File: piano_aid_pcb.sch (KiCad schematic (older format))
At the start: 35 parts, among them J1 Barrel_Jack_MountingPin, J2 796644-3, J3 DIN-5_180degree, J4 Conn_01x06_Female, J5 Micro_SD_Card_Det, J6 Conn_01x07_Female, U1 317030213, U2 6N138, U3 74AHCT1G125W5-7, U4 AZ1117-3.3

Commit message: Made some adjustments. Fixed silkscreen. Added team info.
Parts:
- J1: symbol Connector:Barrel_Jack_MountingPin -> piano_aid_pcb-rescue:Barrel_Jack_MountingPin-Connector
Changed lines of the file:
@@
 $EndComp
 $Comp
-L Connector:Barrel_Jack_MountingPin J1
+L piano_aid_pcb-rescue:Barrel_Jack_MountingPin-Connector J1
 U 1 1 61503033
 P 1150 1350

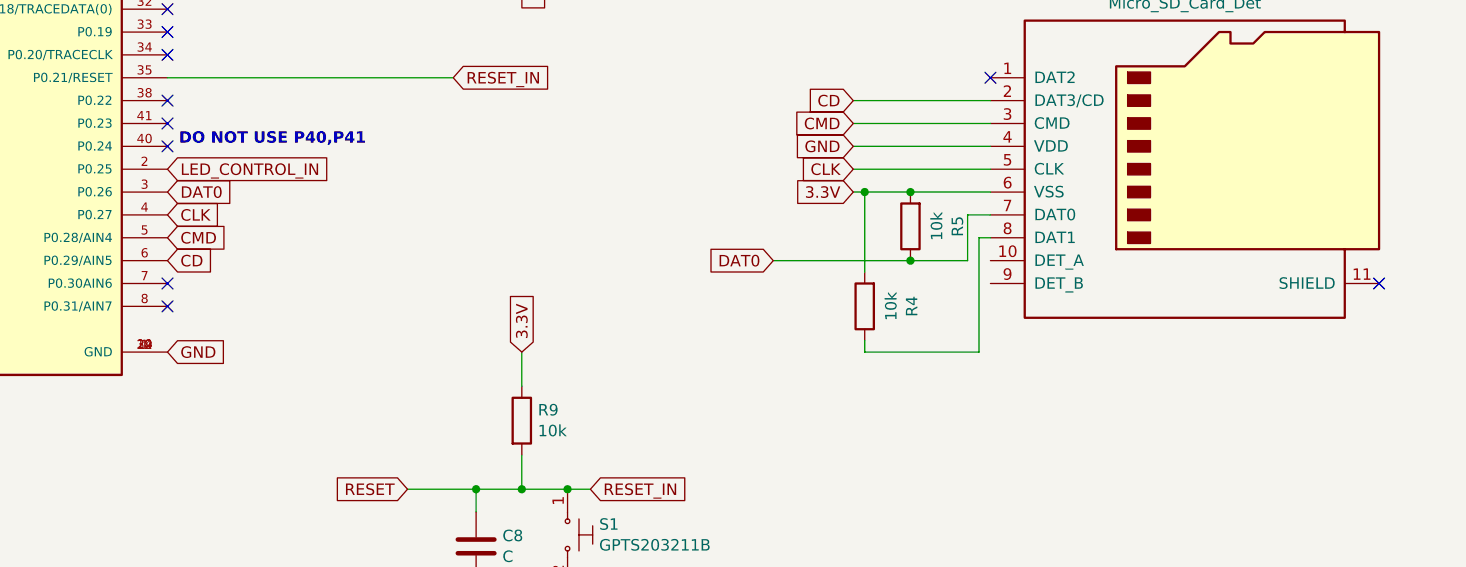
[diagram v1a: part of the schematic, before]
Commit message: Fixed some silkscreen issues. Also fixed microsd footprint and added chip detect functionality
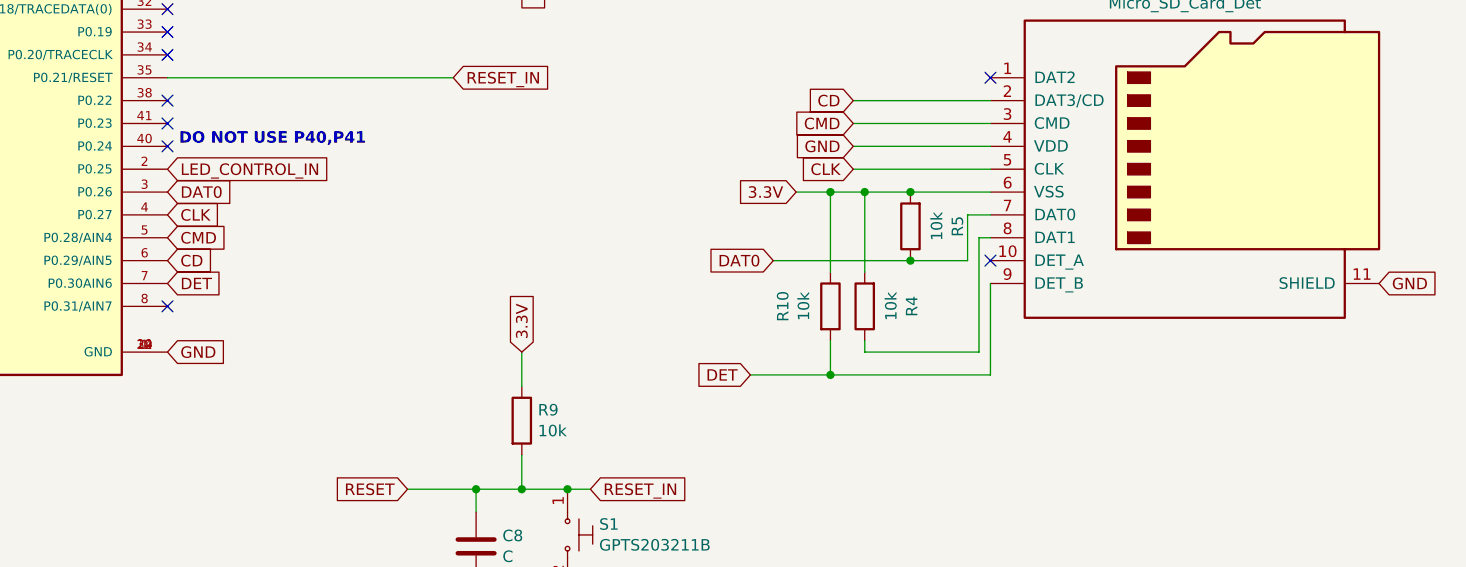
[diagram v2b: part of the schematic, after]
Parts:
- added R10: 10k, Resistor_SMD:R_0805_2012Metric_Pad1.15x1.40mm_HandSolder, symbol Device:R
- J5: footprint adafruit:MICROSD -> microsd:MICROSD
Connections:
- net 3.3V: now also R10.1
- net GND: now also J5.11 (SHIELD)
- net DET: now reaches U1.7 (P0.30AIN6)
- net DET: now also J5.9 (DET_B), R10.2
- no-connect marks 23 -> 22
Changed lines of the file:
@@
 Connection ~ 1700 1500
 Connection ~ 1700 1200
-Text GLabel 8650 4200 0    50   Input ~ 0
+Text GLabel 8400 4200 0    50   Input ~ 0
 3.3V
 Text GLabel 5900 2500 2    50   Input ~ 0
@@
 Wire Wire Line
 	8650 4000 9250 4000
-Wire Wire Line
-	8650 4200 8700 4200
 Connection ~ 8900 4200
 NoConn ~ 9250 3700
@@
 NoConn ~ 5650 3300
 NoConn ~ 5650 3800
-NoConn ~ 5650 4600
 NoConn ~ 5650 4700
 NoConn ~ 3650 3700
@@
 NoConn ~ 5650 2700
 NoConn ~ 5650 2600
-NoConn ~ 10950 4600
 Wire Wire Line
 	7250 2500 7650 2500
@@
 F 3 "~" H 1200 1310 50  0001 C CNN
 	1    1150 1350
-	1    0    0    -1
-$EndComp
-$Comp
-L Connector:Micro_SD_Card_Det J5
-U 1 1 61510C4F
-P 10150 4100
-F 0 "J5" H 10100 4917 50  0000 C CNN
-F 1 "Micro_SD_Card_Det" H 10100 4826 50  0000 C CNN
-F 2 "adafruit:MICROSD" H 12200 4800 50  0001 C CNN
-F 3 "https://www.hirose.com/product/en/download_file/key_name/DM3/category/Catalog/doc_file_id/49662/?file_category_id=4&item_id=195&is_series=1" H 10150 4200 50  0001 C CNN
-	1    10150 4100
 	1    0    0    -1
 $EndComp
@@
 	1    0    0    -1
 $EndComp
+NoConn ~ 9250 4500
+$Comp
+L Device:R R10
+U 1 1 6157C549
+P 8550 4700
+F 0 "R10" V 8343 4700 50  0000 C CNN
+F 1 "10k" V 8434 4700 50  0000 C CNN
+F 2 "Resistor_SMD:R_0805_2012Metric_Pad1.15x1.40mm_HandSolder" V 8480 4700 50  0001 C CNN
+F 3 "~" H 8550 4700 50  0001 C CNN
+	1    8550 4700
+	1    0    0    -1
+$EndComp
+Wire Wire Line
+	8550 4550 8550 4200
+Wire Wire Line
+	8400 4200 8550 4200
+Connection ~ 8550 4200
+Wire Wire Line
+	8550 4200 8700 4200
+Wire Wire Line
+	8550 4850 8550 5000
+Wire Wire Line
+	8550 5000 9250 5000
+Wire Wire Line
+	9250 5000 9250 4600
+Wire Wire Line
+	8550 5000 8200 5000
+Connection ~ 8550 5000
+Text GLabel 8200 5000 0    50   Input ~ 0
+DET
+Text GLabel 5650 4600 2    50   Input ~ 0
+DET
+$Comp
+L Connector:Micro_SD_Card_Det J5
+U 1 1 61510C4F
+P 10150 4100
+F 0 "J5" H 10100 4917 50  0000 C CNN
+F 1 "Micro_SD_Card_Det" H 10100 4826 50  0000 C CNN
+F 2 "microsd:MICROSD" H 12200 4800 50  0001 C CNN
+F 3 "https://www.hirose.com/product/en/download_file/key_name/DM3/category/Catalog/doc_file_id/49662/?file_category_id=4&item_id=195&is_series=1" H 10150 4200 50  0001 C CNN
+	1    10150 4100
+	1    0    0    -1
+$EndComp
+Text GLabel 10950 4600 2    50   Input ~ 0
+GND
 $EndSCHEMATC

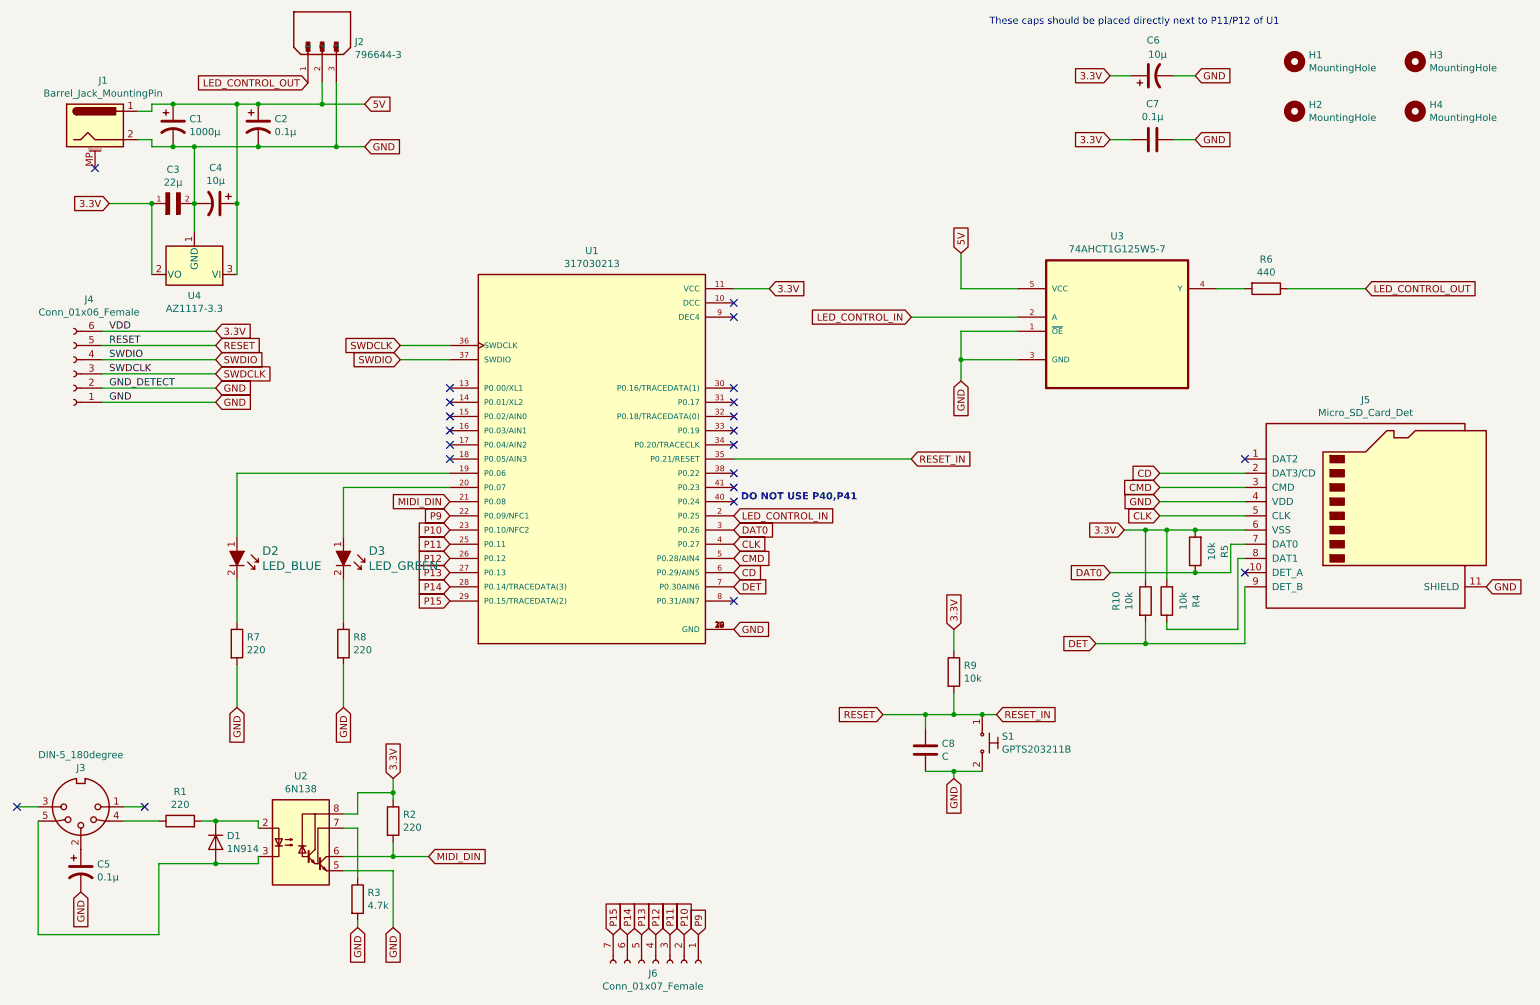
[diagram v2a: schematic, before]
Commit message: Changed out barrel jack. Still needs to be connected to ground. I think there's an issue with the footprint. Also rounded the edges of the board.
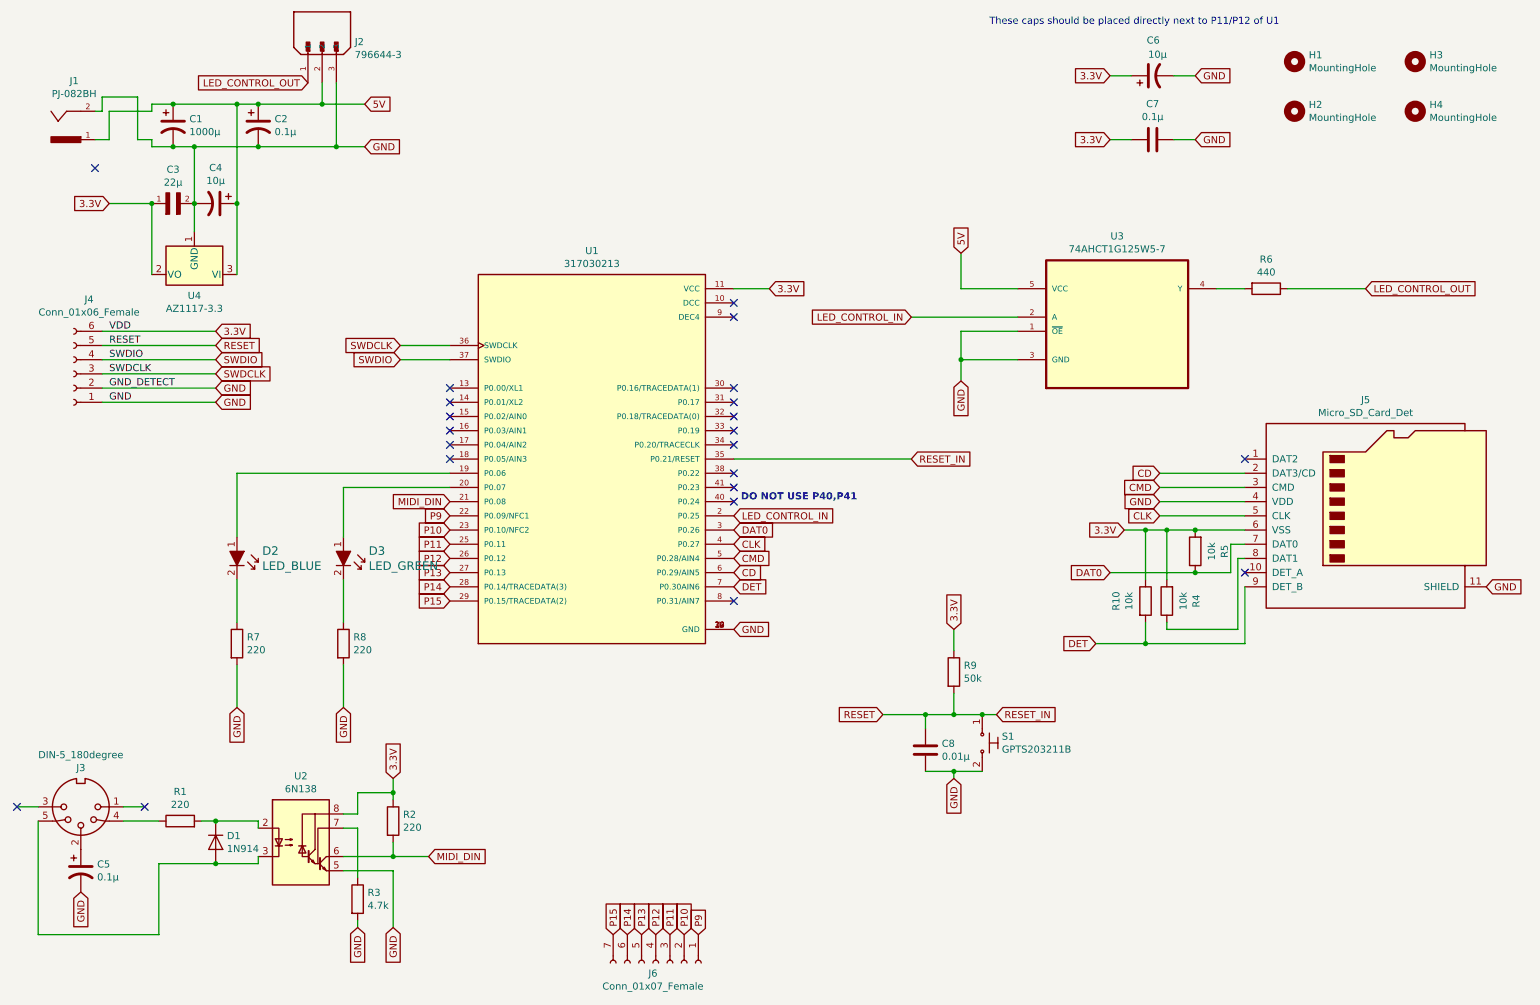
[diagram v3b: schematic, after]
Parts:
- removed J1: Barrel_Jack_MountingPin, Connector_BarrelJack:BarrelJack_Horizontal, symbol piano_aid_pcb-rescue:Barrel_Jack_MountingPin-Connector
- added J1: PJ-082BH, PJ-082BH:CUI_PJ-082BH, symbol PJ-082BH:PJ-082BH
- C8: value C -> 0.01µ
- R9: value 10k -> 50k
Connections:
- net 5V: now also J1.1
- net GND: now also J1.2
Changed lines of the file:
@@
 $EndComp
-Wire Wire Line
-	1450 1250 1550 1250
 Wire Wire Line
 	1550 1250 1550 1200
@@
 F 5 "Seeed Technology Co" H 4650 3700 50  0001 L BNN "MANUFACTURER"
 	1    4650 3700
-	1    0    0    -1
-$EndComp
-$Comp
-L piano_aid_pcb-rescue:Barrel_Jack_MountingPin-Connector J1
-U 1 1 61503033
-P 1150 1350
-F 0 "J1" H 1207 1667 50  0000 C CNN
-F 1 "Barrel_Jack_MountingPin" H 1207 1576 50  0000 C CNN
-F 2 "Connector_BarrelJack:BarrelJack_Horizontal" H 1200 1310 50  0001 C CNN
-F 3 "~" H 1200 1310 50  0001 C CNN
-	1    1150 1350
 	1    0    0    -1
 $EndComp
@@
 P 7200 5200
 F 0 "R9" H 7270 5246 50  0000 L CNN
-F 1 "10k" H 7270 5155 50  0000 L CNN
+F 1 "50k" H 7270 5155 50  0000 L CNN
 F 2 "Resistor_SMD:R_0805_2012Metric_Pad1.15x1.40mm_HandSolder" V 7130 5200 50  0001 C CNN
 F 3 "~" H 7200 5200 50  0001 C CNN
@@
 P 7000 5750
 F 0 "C8" H 7115 5796 50  0000 L CNN
-F 1 "C" H 7115 5705 50  0000 L CNN
+F 1 "0.01µ" H 7115 5705 50  0000 L CNN
 F 2 "Capacitor_SMD:C_0805_2012Metric_Pad1.15x1.40mm_HandSolder" H 7038 5600 50  0001 C CNN
 F 3 "~" H 7000 5750 50  0001 C CNN
@@
 Text GLabel 10950 4600 2    50   Input ~ 0
 GND
+$Comp
+L PJ-082BH:PJ-082BH J1
+U 1 1 61572DF0
+P 950 1350
+F 0 "J1" H 897 1036 50  0000 C CNN
+F 1 "PJ-082BH" H 897 1127 50  0000 C CNN
+F 2 "PJ-082BH:CUI_PJ-082BH" H 950 1350 50  0001 L BNN
+F 3 "" H 950 1350 50  0001 L BNN
+F 4 "CUI Inc" H 950 1350 50  0001 L BNN "MANUFACTURER"
+	1    950  1350
+	-1   0    0    1
+$EndComp
+Wire Wire Line
+	1150 1450 1250 1450
+Wire Wire Line
+	1250 1450 1250 1250
+Wire Wire Line
+	1250 1250 1550 1250
+Wire Wire Line
+	1150 1250 1200 1250
+Wire Wire Line
+	1200 1250 1200 1150
+Wire Wire Line
+	1200 1150 1450 1150
+Wire Wire Line
+	1450 1150 1450 1450
 $EndSCHEMATC

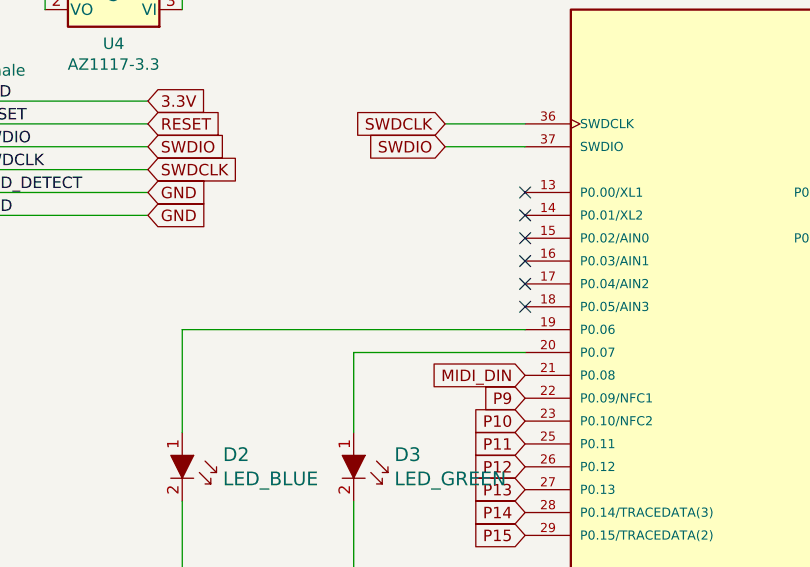
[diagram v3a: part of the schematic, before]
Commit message: Fixed absolute paths, added pull up resistor.
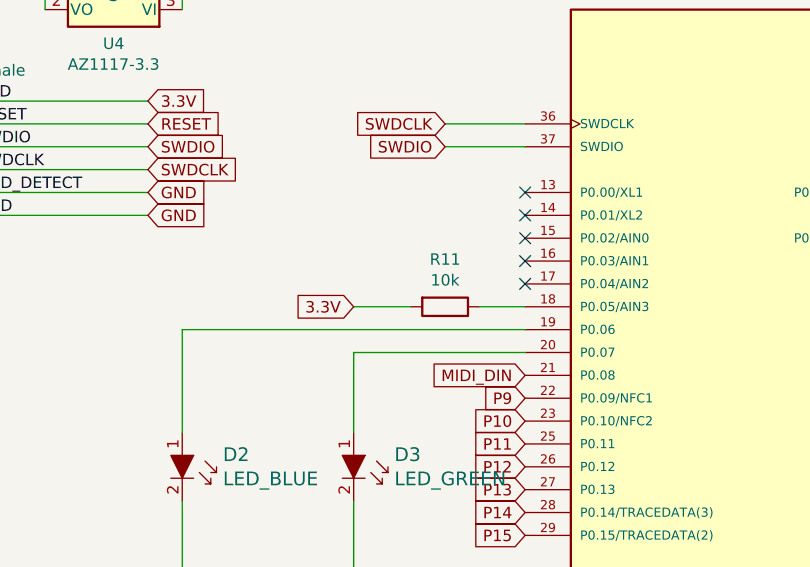
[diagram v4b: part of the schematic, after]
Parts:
- added R11: 10k, Resistor_SMD:R_0805_2012Metric_Pad1.15x1.40mm_HandSolder, symbol Device:R
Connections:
- net 3.3V: now also R11.2
- net at U1.18 (P0.05/AIN3): now also R11.1
- no-connect marks 22 -> 21
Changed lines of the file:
@@
 NoConn ~ 5650 3800
 NoConn ~ 5650 4700
-NoConn ~ 3650 3700
 NoConn ~ 3650 3600
 NoConn ~ 3650 3500
@@
 Wire Wire Line
 	1450 1150 1450 1450
+$Comp
+L Device:R R11
+U 1 1 615CBC31
+P 3300 3700
+F 0 "R11" V 3093 3700 50  0000 C CNN
+F 1 "10k" V 3184 3700 50  0000 C CNN
+F 2 "Resistor_SMD:R_0805_2012Metric_Pad1.15x1.40mm_HandSolder" V 3230 3700 50  0001 C CNN
+F 3 "~" H 3300 3700 50  0001 C CNN
+	1    3300 3700
+	0    1    1    0
+$EndComp
+Wire Wire Line
+	3450 3700 3650 3700
+Text GLabel 2900 3700 0    50   Input ~ 0
+3.3V
+Wire Wire Line
+	2900 3700 3150 3700
 $EndSCHEMATC
